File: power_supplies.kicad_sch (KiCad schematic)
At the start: 40 parts, among them IC1 ECP5-BGA256, U1 TLV62569ADRLR, U2 NCP115-2.5, U4 NCP115-1.8

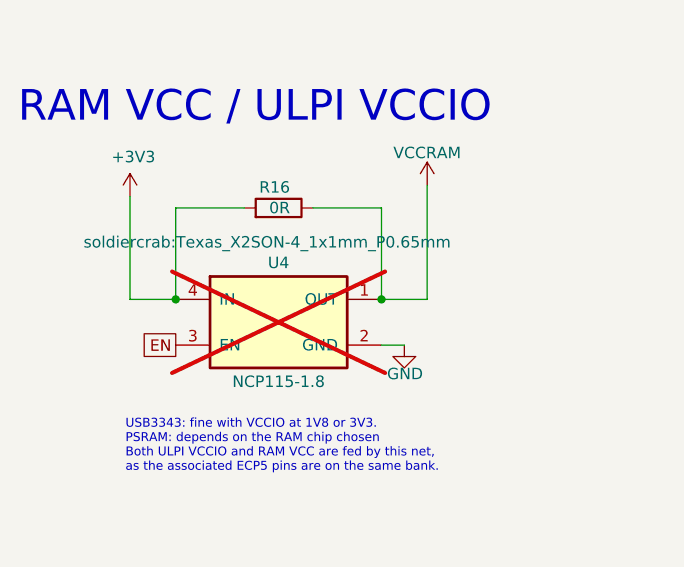
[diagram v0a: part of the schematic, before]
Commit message: kicad: fix LED PD, APMem, 1V8, USB ~RST short
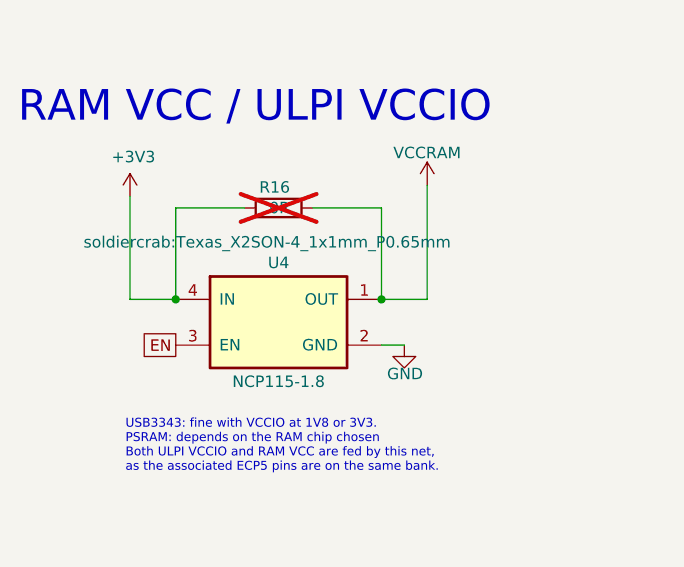
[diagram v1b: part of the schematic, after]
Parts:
- R16: now not fitted
- U4: now fitted
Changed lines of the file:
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@@
 		(in_bom yes)
 		(on_board yes)
-		(dnp no)
+		(dnp yes)
 		(property "Reference" "R16"
 			(at 49.53 94.234 90)
@@
 		(in_bom yes)
 		(on_board yes)
-		(dnp yes)
+		(dnp no)
 		(property "Reference" "U4"
 			(at 48.26 102.616 0)
